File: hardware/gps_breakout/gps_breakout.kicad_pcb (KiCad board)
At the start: 2 copper layers, 33 parts, among them CON1 USB-MICRO-B, P1 CONN_01X06, P2 CONN_02X07, P3 CONN_01X03, P4 CONN_01X03, P5 CONN_01X03, U1 MCP1700, U2 CY7C65213, U3 M10478-A3

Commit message: finished layout of gps board
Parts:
- C5: value 100nF -> 1000nF
- P1: moved to B.Cu
- P3, P4, P5: footprint Connect:PINHEAD1-3 -> sensornode:JMP_HDR
- moved U3 39.2 mm to (126.5, 115.0), turned to 180 degrees
- moved C13 35.2 mm to (118.2, 123.0), turned to 270 degrees
- moved L3 32.4 mm to (119.2, 119.0), turned to 180 degrees
- moved L4 31.6 mm to (119.2, 117.0), turned to 180 degrees
- moved R4 30.8 mm to (118.2, 99.8), turned to 90 degrees
- moved D3 30.4 mm to (118.2, 102.9), turned to 90 degrees
- moved L1 24.7 mm to (134.0, 125.0), turned to 90 degrees
- moved P5 23.9 mm to (137.2, 117.5)
- moved U2 23.5 mm to (144.8, 119.2)
- moved L2 23.2 mm to (136.7, 125.0), turned to 90 degrees
- moved C11 22.6 mm to (126.5, 110.0), turned to 180 degrees
- moved C8 22.2 mm to (134.0, 121.8), turned to 90 degrees
- moved CON1 19.8 mm to (162.2, 120.8)
- moved C10 19.4 mm to (129.8, 110.0)
- moved C9 19.3 mm to (133.9, 117.6), turned to 90 degrees
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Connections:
- P2 pad 1: /RST -> /MSP_RST
- P2 pad 7: /TCK -> /MSP_TST
- U3 pad 10: Net-(P5-Pad3) -> Net-(P5-Pad2)
- U3 pad 11: Net-(P5-Pad2) -> Net-(P5-Pad3)
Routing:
- net +3V3: track 0.00 -> 113.3 mm, vias 0 -> 4
- net GND: track 0.00 -> 82.8 mm, vias 0 -> 36
- net /GPS_TXD: track 0.00 -> 37.0 mm, vias 0 -> 3
- net +5V: track 0.00 -> 35.4 mm, vias 0 -> 2
- net /MSP_RST: track 0.00 -> 33.1 mm, vias 0 -> 2
- net /GPS_RXD: track 0.00 -> 30.9 mm, vias 0 -> 2
- net /MSP_TXD: track 0.00 -> 27.6 mm, vias 0 -> 2
- net /MSP_TST: track 0.00 -> 20.3 mm, vias 0 -> 1
- net /MSP_RXD: track 0.00 -> 19.4 mm
- net Net-(D3-Pad1): track 0.00 -> 14.6 mm, vias 0 -> 2
- net Net-(CON1-Pad3): track 0.00 -> 14.4 mm, vias 0 -> 2
- net /CY_RXD: track 0.00 -> 13.5 mm
- net Net-(CON1-Pad2): track 0.00 -> 13.1 mm
- net /CY_TXD: track 0.00 -> 10.7 mm
- net Net-(C8-Pad2): track 0.00 -> 8.18 mm
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- added copper zone on B.Cu, net GND
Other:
- board outline added: 49 x 29 mm
- board text added: "3v3"
- board text added: "ee646 sensor network project gps/jtag adapter/usb-uart"
- board text added: "gnd"
- board text added: "gps"
- board text added: "gps link"
- board text added: "jtag"
- board text added: "msp"
- board text added: "pps rst gnd"
- board text added: "rst"
- board text added: "rxd"
- board text added: "tst"
- board text added: "txd"

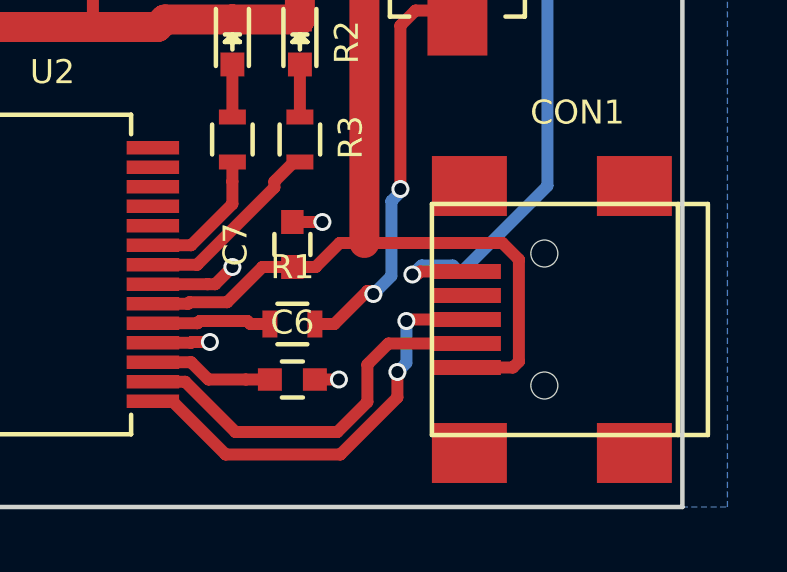
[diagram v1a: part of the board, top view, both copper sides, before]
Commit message: ordered gps board
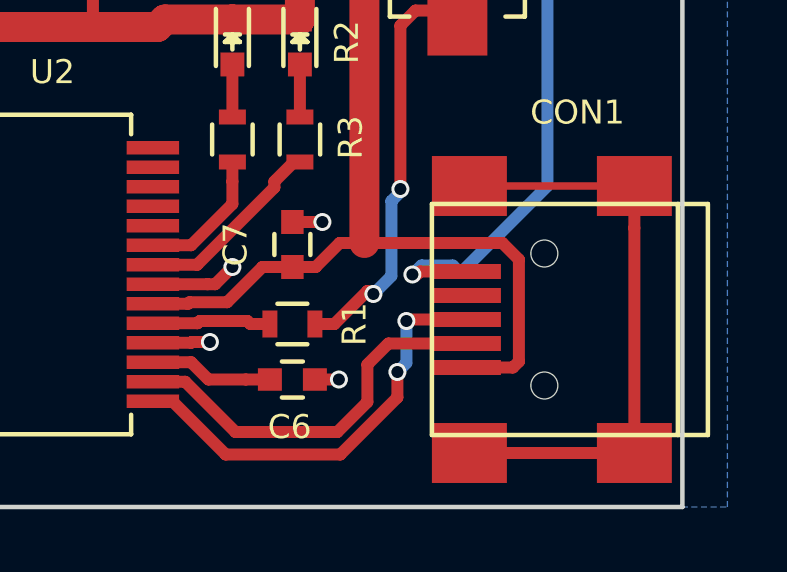
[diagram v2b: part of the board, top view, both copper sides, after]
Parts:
- added U4: silkscreen_label, sensornode:gunter, B.Cu at (144.9, 116.7)
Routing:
- net Net-(CON1-Pad6): track 0.00 -> 19.9 mm
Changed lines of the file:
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@@
   (general
     (links 88)
-    (no_connects 4)
-    (area 116.924999 97.924999 166.075001 127.075001)
+    (no_connects 0)
+    (area 111.825 95.5 167.500001 130.685)
     (thickness 1.6)
     (drawings 20)
-    (tracks 370)
+    (tracks 374)
     (zones 0)
-    (modules 33)
+    (modules 34)
     (nets 59)
   )
@@
   )
   (setup
-    (last_trace_width 0.4)
+    (last_trace_width 0.25)
     (user_trace_width 0.4)
     (user_trace_width 1)
@@
     (visible_elements FFFEFF7F)
     (pcbplotparams
-      (layerselection 0x00030_80000001)
+      (layerselection 0x010f0_80000001)
       (usegerberextensions false)
       (excludeedgelayer true)
@@
       (outputformat 1)
       (mirror false)
-      (drillshape 1)
+      (drillshape 0)
       (scaleselection 1)
-      (outputdirectory ""))
+      (outputdirectory gerbs/))
   )
   (net 0 "")
@@
     (tags "capacitor 0603")
     (attr smd)
-    (fp_text reference C6 (at 0 -1.9) (layer F.SilkS)
+    (fp_text reference C6 (at -0.092 1.583) (layer F.SilkS)
       (effects (font (size 0.8 0.8) (thickness 0.15)))
     )
@@
     (tags "resistor 0603")
     (attr smd)
-    (fp_text reference R1 (at 0 -1.9) (layer F.SilkS)
+    (fp_text reference R1 (at 2.067 0.004 90) (layer F.SilkS)
       (effects (font (size 0.8 0.8) (thickness 0.15)))
     )
@@
     (pad 3 thru_hole circle (at 2.54 0 90) (size 1.524 1.524) (drill 1) (layers *.Cu *.Mask F.SilkS)
       (net 37 "Net-(P5-Pad3)"))
+  )
+  (module sensornode:gunter (layer B.Cu)
+    (at 144.907 116.713 180)
+    (fp_text reference U4 (at 0 0 180) (layer B.SilkS) hide
+      (effects (font (thickness 0.3)) (justify mirror))
+    )
+    (fp_text value silkscreen_label (at 0.75 0 180) (layer B.SilkS) hide
+      (effects (font (thickness 0.3)) (justify mirror))
+    )
+    (fp_poly (pts (xy -1.062264 7.557002) (xy -0.50955 7.461223) (xy -0.000417 7.303962) (xy 0.132801 7.247235)
+      (xy 0.689606 6.926207) (xy 1.129652 6.517865) (xy 1.467138 6.002899) (xy 1.716265 5.362001)
+      (xy 1.819866 4.953) (xy 1.896573 4.48201) (xy 1.95574 3.882653) (xy 1.996244 3.1951)
+      (xy 2.016964 2.459518) (xy 2.016779 1.716078) (xy 1.994566 1.004948) (xy 1.949204 0.366298)
+      (xy 1.948217 0.356204) (xy 1.899957 -0.102178) (xy 1.854233 -0.430176) (xy 1.801396 -0.666303)
+      (xy 1.731798 -0.849068) (xy 1.635789 -1.016983) (xy 1.585282 -1.092323) (xy 1.322768 -1.490675)
+      (xy 1.041595 -1.945631) (xy 0.760765 -2.423384) (xy 0.499283 -2.890128) (xy 0.27615 -3.312058)
+      (xy 0.110372 -3.655368) (xy 0.027907 -3.862775) (xy -0.048802 -4.125628) (xy -0.068766 -4.290709)
+      (xy -0.031113 -4.420098) (xy 0.037343 -4.533933) (xy 0.118882 -4.645842) (xy 0.209919 -4.710968)
+      (xy 0.352305 -4.738867) (xy 0.587891 -4.739094) (xy 0.876446 -4.725518) (xy 1.566334 -4.689372)
+      (xy 1.588169 -5.443644) (xy 1.651139 -6.23443) (xy 1.787492 -6.998897) (xy 1.987091 -7.698277)
+      (xy 2.2398 -8.293803) (xy 2.407636 -8.577707) (xy 2.606526 -8.870788) (xy 2.298096 -8.921796)
+      (xy 2.023473 -8.948274) (xy 1.617512 -8.963241) (xy 1.117762 -8.967456) (xy 0.561773 -8.961678)
+      (xy -0.012904 -8.946667) (xy -0.568721 -8.923181) (xy -1.068127 -8.89198) (xy -1.473572 -8.853822)
+      (xy -1.550726 -8.843987) (xy -2.352995 -8.72273) (xy -2.999924 -8.59901) (xy -3.487376 -8.473786)
+      (xy -3.811215 -8.348022) (xy -3.890915 -8.300005) (xy -4.133555 -8.033205) (xy -4.337683 -7.610467)
+      (xy -4.499378 -7.041614) (xy -4.585609 -6.559034) (xy -4.611822 -6.285623) (xy -4.634837 -5.865899)
+      (xy -4.654543 -5.322856) (xy -4.670829 -4.679484) (xy -4.683582 -3.958779) (xy -4.692693 -3.183731)
+      (xy -4.698048 -2.377333) (xy -4.699538 -1.562579) (xy -4.697051 -0.762461) (xy -4.690476 0.000029)
+      (xy -4.679701 0.701897) (xy -4.664615 1.320152) (xy -4.645106 1.831801) (xy -4.627665 2.129549)
+      (xy -4.55633 3.116099) (xy -3.394376 3.070101) (xy -2.232421 3.024102) (xy -2.047544 3.259136)
+      (xy -1.892997 3.52297) (xy -1.891524 3.758318) (xy -2.044075 4.011068) (xy -2.06358 4.034133)
+      (xy -2.233006 4.190408) (xy -2.424711 4.248003) (xy -2.613913 4.247091) (xy -2.835055 4.24211)
+      (xy -2.93525 4.284258) (xy -2.962293 4.406501) (xy -2.962745 4.442039) (xy -1.27 4.442039)
+      (xy -1.208858 3.997325) (xy -1.033149 3.648759) (xy -0.782102 3.434536) (xy -0.453496 3.330727)
+      (xy -0.05724 3.309381) (xy 0.327837 3.368549) (xy 0.56739 3.467905) (xy 0.87662 3.74114)
+      (xy 1.046852 4.077121) (xy 1.079448 4.443873) (xy 0.975772 4.809421) (xy 0.737187 5.141788)
+      (xy 0.487607 5.339487) (xy 0.25577 5.44953) (xy -0.009575 5.487077) (xy -0.246783 5.478757)
+      (xy -0.540597 5.441429) (xy -0.742473 5.359901) (xy -0.929589 5.19853) (xy -0.987616 5.136621)
+      (xy -1.171116 4.90382) (xy -1.253341 4.684155) (xy -1.27 4.442039) (xy -2.962745 4.442039)
+      (xy -2.963333 4.488108) (xy -3.004489 4.762412) (xy -3.086604 4.988121) (xy -3.260611 5.192822)
+      (xy -3.524868 5.374689) (xy -3.804045 5.487393) (xy -3.924309 5.503333) (xy -4.001146 5.520223)
+      (xy -4.006881 5.599446) (xy -3.941878 5.783829) (xy -3.927007 5.820833) (xy -3.783194 6.115373)
+      (xy -3.579745 6.456894) (xy -3.349137 6.797869) (xy -3.123844 7.090771) (xy -2.936345 7.288074)
+      (xy -2.910064 7.309063) (xy -2.582459 7.467329) (xy -2.138661 7.560866) (xy -1.618615 7.590487)
+      (xy -1.062264 7.557002)) (layer B.SilkS) (width 0.01))
+    (fp_poly (pts (xy -2.367662 4.091825) (xy -2.175041 3.951522) (xy -2.050287 3.754694) (xy -2.032 3.651814)
+      (xy -2.075192 3.540385) (xy -2.229042 3.470768) (xy -2.391833 3.43981) (xy -2.661327 3.409829)
+      (xy -3.027361 3.383282) (xy -3.456455 3.36101) (xy -3.915132 3.343851) (xy -4.369914 3.332644)
+      (xy -4.787323 3.32823) (xy -5.133882 3.331448) (xy -5.376111 3.343137) (xy -5.478509 3.362415)
+      (xy -5.43613 3.406038) (xy -5.232829 3.479671) (xy -4.874071 3.581884) (xy -4.365324 3.711248)
+      (xy -3.712054 3.866334) (xy -2.919728 4.045713) (xy -2.568504 4.123198) (xy -2.367662 4.091825)) (layer B.SilkS) (width 0.01))
+    (fp_poly (pts (xy -4.052834 5.259238) (xy -4.013433 5.210057) (xy -3.915217 5.044301) (xy -3.924707 4.912691)
+      (xy -4.053948 4.756288) (xy -4.118696 4.694957) (xy -4.341669 4.551315) (xy -4.579544 4.49058)
+      (xy -4.779385 4.517881) (xy -4.882586 4.620944) (xy -4.868802 4.79326) (xy -4.746791 4.997639)
+      (xy -4.555955 5.183202) (xy -4.364617 5.28974) (xy -4.17645 5.328943) (xy -4.052834 5.259238)) (layer B.SilkS) (width 0.01))
+    (fp_poly (pts (xy -0.269386 5.139592) (xy -0.135398 5.018468) (xy -0.128015 4.998531) (xy -0.129328 4.762238)
+      (xy -0.251396 4.536597) (xy -0.452229 4.355871) (xy -0.689835 4.254325) (xy -0.922223 4.266221)
+      (xy -0.986371 4.29813) (xy -1.10317 4.458523) (xy -1.105835 4.675015) (xy -1.00784 4.892392)
+      (xy -0.822656 5.055439) (xy -0.798722 5.067151) (xy -0.501946 5.156991) (xy -0.269386 5.139592)) (layer B.SilkS) (width 0.01))
   )
   (gr_line (start 141.605 98.425) (end 141.605 99.695) (layer F.SilkS) (width 0.2))
@@
   (segment (start 148.35 123.475) (end 149 123.475) (width 0.4) (layer F.Cu) (net 10))
   (segment (start 149 123.475) (end 150.775 125.25) (width 0.4) (layer F.Cu) (net 10))
+  (segment (start 164.39884 125.20008) (end 158.89974 125.20008) (width 0.4) (layer F.Cu) (net 12))
+  (segment (start 164.39884 116.29992) (end 164.39884 117.69941) (width 0.4) (layer F.Cu) (net 12))
+  (segment (start 164.39884 117.69941) (end 164.39884 125.20008) (width 0.4) (layer F.Cu) (net 12))
+  (segment (start 158.89974 116.29992) (end 164.39884 116.29992) (width 0.25) (layer F.Cu) (net 12))
   (segment (start 151 114) (end 151 112.2486) (width 0.4) (layer F.Cu) (net 13))
   (segment (start 153.25 112.2493) (end 153.25 114) (width 0.4) (layer F.Cu) (net 14))
